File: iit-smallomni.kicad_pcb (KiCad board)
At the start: 2 copper layers, 100 x 100 mm, 87 parts, among them J1 Battery, J10 DC-Motor, J2 HC_SR04, J3 HC_SR04, J4 HC_SR04, J5 DC-Motor, J6 DC-Motor, J7 DC-Motor, J8 DC-Motor, J9 DC-Motor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

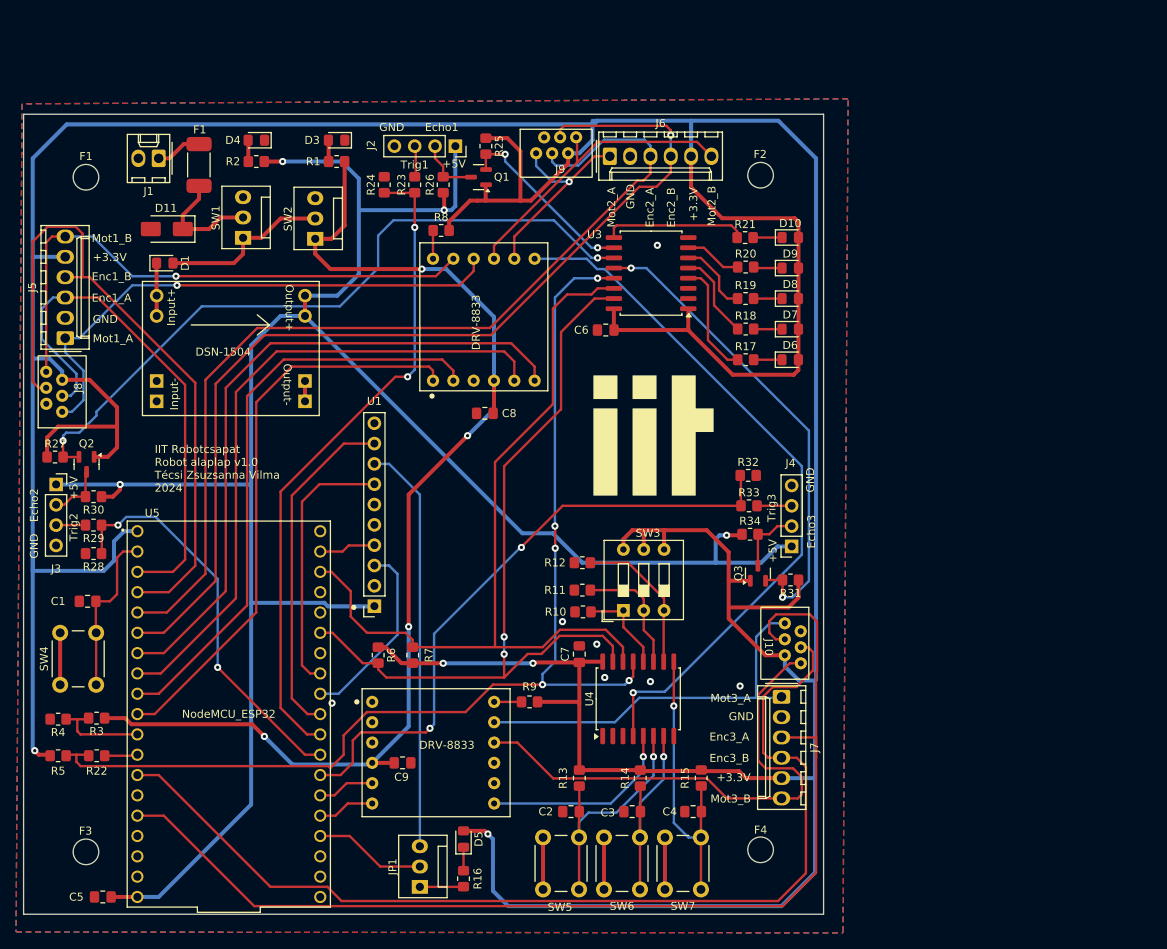
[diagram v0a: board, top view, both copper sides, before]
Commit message: Clean up names, schematic grid and files
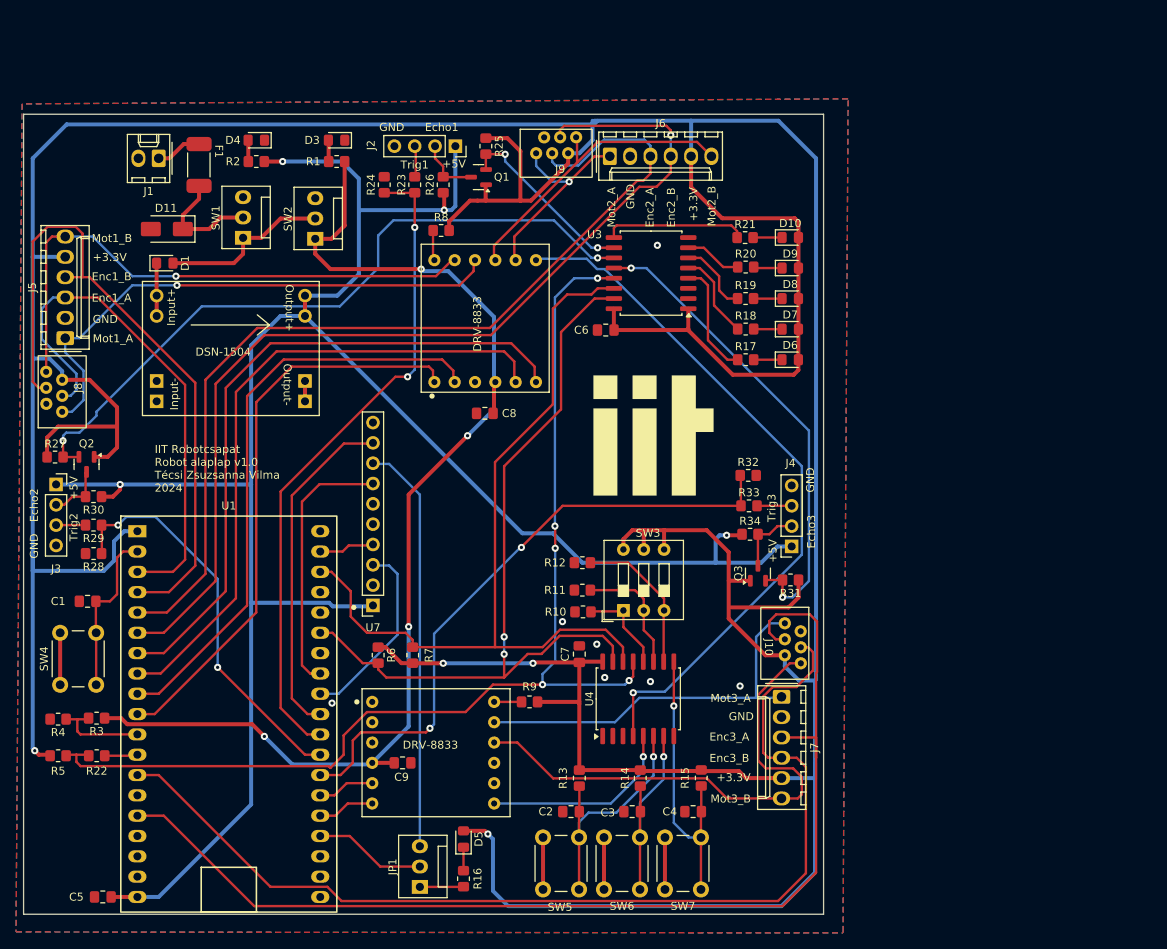
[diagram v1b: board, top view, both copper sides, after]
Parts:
- removed the F1 at (122.1, 34.9)
- removed F2, F3, F4: MountingHole_3.2mm_M3, MountingHole:MountingHole_3.2mm_M3
- F1: footprint Onlab:polyfuse -> iit-smallomni:polyfuse
- J10, J8, J9: footprint Onlab:motor -> iit-smallomni:motor
- R1: value 502.5 -> 10k
- R16, R17, R18, R19, R20, R21: value 68 -> 1k
- R2: value 152.5 -> 3k
- R3: value 7.5k -> 9.1k
- R4: value 2.5k -> 3k
- U1: value MPU-9250_IMU -> NodeMCU_ESP32; footprint Connector_PinSocket_2.54mm:PinSocket_1x10_P2.54mm_Vertical -> iit-smallomni:NodeMCU32S
- U2: footprint Onlab:DSN1504_module -> iit-smallomni:DSN1504_module
- U5: value NodeMCU_ESP32 -> DRV-8833_module; footprint NodeMCU_ESP32:MODULE_NODEMCU-32S -> iit-smallomni:DRV-8833_module
- U6: footprint Onlab:DRV-8833_module -> iit-smallomni:DRV-8833_module
- U7: value DRV-8833_module -> MPU-9250_IMU; footprint Onlab:DRV-8833_module -> Connector_PinSocket_2.54mm:PinSocket_1x10_P2.54mm_Vertical
- moved U5 57.4 mm to (171.6, 54.1), turned to 90 degrees
- moved U7 37.0 mm to (158.0, 88.4), turned to 180 degrees
- moved U1 22.7 mm to (140.0, 102.0), turned to 0 degrees
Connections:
- C1 pad 1: Net-(U5-EN/RESET) -> Net-(U1-EN/RESET)
- R22 pad 2: Net-(U5-P14/GPIO14/ADC2_CH6) -> Net-(U1-P14/GPIO14/ADC2_CH6)
- R8 pad 2: Net-(U7-EEP) -> Net-(U5-EEP)
- SW4 pad 2: Net-(U5-EN/RESET) -> Net-(U1-EN/RESET)
- U1 pad 1: +5V -> +3.3V
- U1 pad 10: GND -> /Mot1_DrvA
- U1 pad 2: GND -> Net-(U1-EN/RESET)
- U1 pad 3: /SCLK -> /Mot1_EncA
- U1 pad 4: /MOSI -> /Mot1_EncB
- U1 pad 5: unconnected-(U1-EDA-Pad5) -> /Mot2_EncA
- U1 pad 6: unconnected-(U1-ECL-Pad6) -> /Mot2_EncB
- U1 pad 7: /MISO -> /Mot2_DrvB
- U1 pad 8: /MPU95 interrupt -> /Mot2_DrvA
- U1 pad 9: /nCS -> /Mot1_DrvB
- U5 pad 1: +3.3V -> /Mot1_DrvA
- U5 pad 10: /Mot1_DrvA -> /Mot1_A
- U5 pad 11: /Battery level -> /Mot1_B
- U5 pad 12: Net-(U5-P14/GPIO14/ADC2_CH6) -> Net-(U5-EEP)
- U5 pad 2: Net-(U5-EN/RESET) -> /Mot1_DrvB
- U5 pad 3: /Mot1_EncA -> GND
- U5 pad 4: /Mot1_EncB -> VCC
- U5 pad 5: /Mot2_EncA -> /Mot2_DrvA
- U5 pad 6: /Mot2_EncB -> /Mot2_DrvB
- U5 pad 7: /Mot2_DrvB -> /DRV1_FAULT
- U5 pad 8: /Mot2_DrvA -> /Mot2_A
- U5 pad 9: /Mot1_DrvB -> /Mot2_B
- U7 pad 1: /Mot1_DrvA -> +5V
- U7 pad 10: /Mot1_A -> GND
- U7 pad 2: /Mot1_DrvB -> GND
- U7 pad 3: GND -> /SCLK
- U7 pad 4: VCC -> /MOSI
- U7 pad 5: /Mot2_DrvA -> unconnected-(U7-EDA-Pad5)
- U7 pad 6: /Mot2_DrvB -> unconnected-(U7-ECL-Pad6)
- U7 pad 7: /DRV1_FAULT -> /MISO
- U7 pad 8: /Mot2_A -> /MPU95 interrupt
- U7 pad 9: /Mot2_B -> /nCS
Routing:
- net Net-(U5-EN/RESET): track 20.9 -> 0.00 mm
- net Net-(U1-EN/RESET): track 0.00 -> 20.9 mm
- net Net-(U5-P14/GPIO14/ADC2_CH6): track 4.19 -> 0.00 mm
- net Net-(U1-P14/GPIO14/ADC2_CH6): track 0.00 -> 4.19 mm
- net Net-(U7-EEP): track 3.54 -> 0.00 mm
- net Net-(U5-EEP): track 0.00 -> 3.54 mm

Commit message: Fix flipped DRV8833
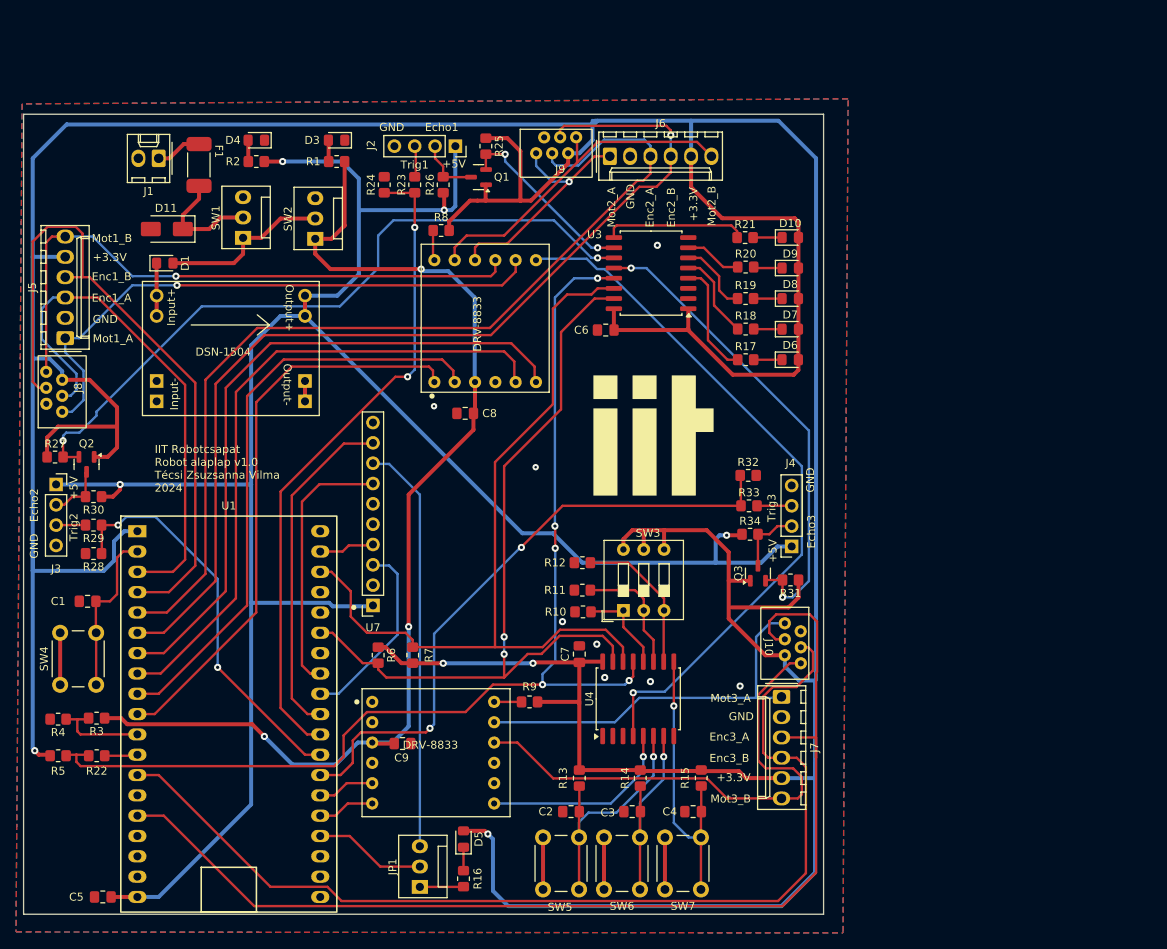
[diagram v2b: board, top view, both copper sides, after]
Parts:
- C1: value 10n -> 10u
- moved C8 2.46 mm to (169.5, 64.4)
- moved C9 2.41 mm to (161.7, 105.7)
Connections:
- U5 pad 10: /Mot1_A -> /Mot2_A
- U5 pad 11: /Mot1_B -> /Mot2_B
- U5 pad 3: GND -> VCC
- U5 pad 4: VCC -> GND
- U5 pad 8: /Mot2_A -> /Mot1_A
- U5 pad 9: /Mot2_B -> /Mot1_B
- U6 pad 3: GND -> VCC
- U6 pad 4: VCC -> GND
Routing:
- net /Mot1_B: track 70.3 -> 76.3 mm
- net VCC: track 144.7 -> 138.9 mm, vias 4 -> 3
- net /Mot1_A: track 68.0 -> 73.1 mm
- net /Mot2_B: track 38.2 -> 43.1 mm
- net /Mot2_A: track 25.4 -> 29.7 mm
- net GND: track 29.2 -> 28.8 mm, vias 7 -> 8

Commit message: Fix flipped DSN-1504
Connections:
- U2 pad 1: GND -> Net-(D1-K)
- U2 pad 2: Net-(D1-K) -> GND
- U2 pad 3: +5V -> GND
- U2 pad 4: GND -> +5V
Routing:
- net Net-(D1-K): track 6.61 -> 19.7 mm, vias 0 -> 1
- net +5V: track 269.3 -> 263.2 mm
- net /UV_Trig_2: track 89.7 -> 94.1 mm
- net GND: track 28.8 -> 26.2 mm, vias 8 -> 10

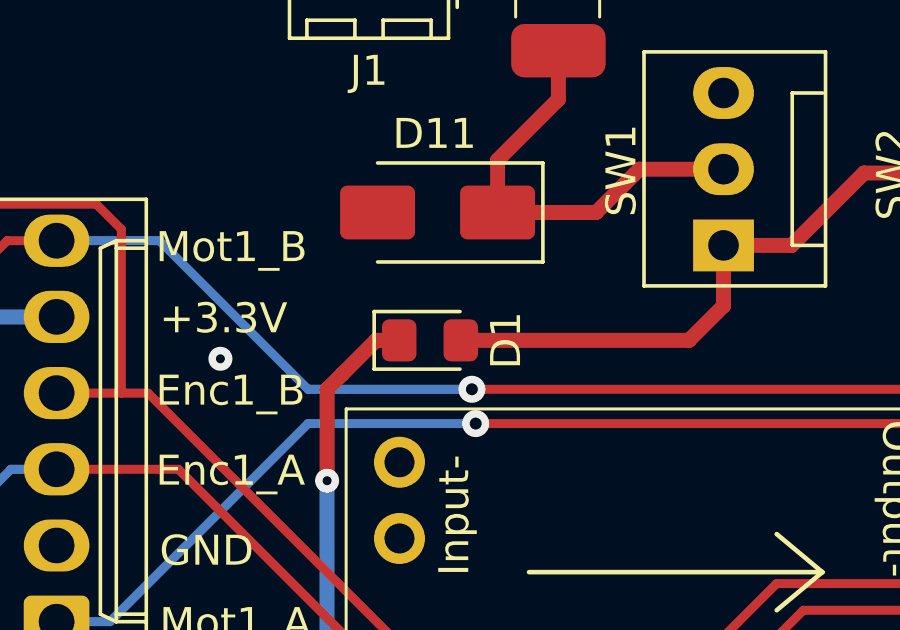
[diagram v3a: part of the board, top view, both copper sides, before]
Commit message: Update Schottky diode footprint in design
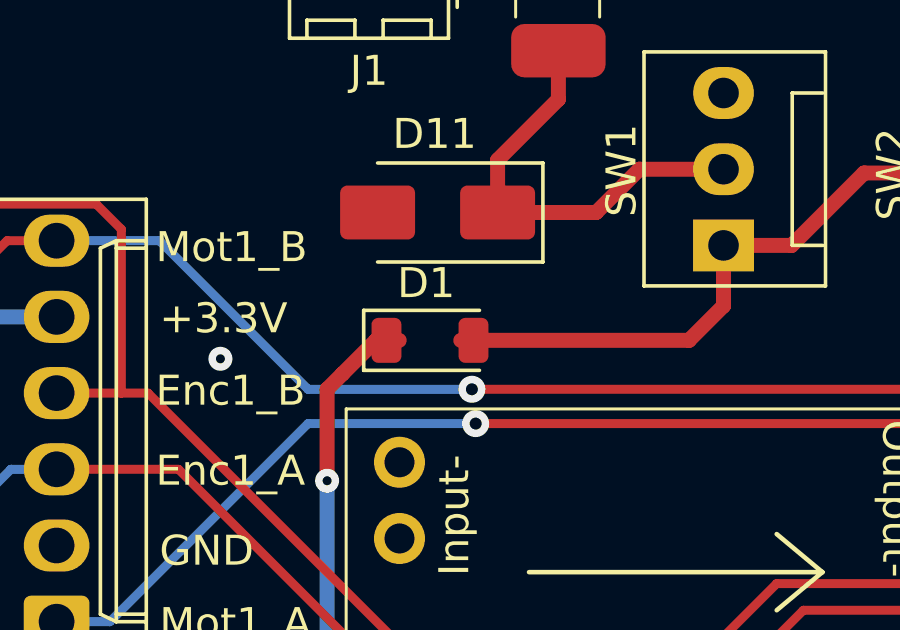
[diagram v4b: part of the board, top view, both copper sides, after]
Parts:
- D1: footprint Diode_SMD:D_0805_2012Metric_Pad1.15x1.40mm_HandSolder -> iit-smallomni:D_SOD-123FL
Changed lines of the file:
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@@
 		)
 	)
-	(footprint "Diode_SMD:D_0805_2012Metric_Pad1.15x1.40mm_HandSolder"
+	(footprint "iit-smallomni:D_SOD-123FL"
 		(layer "F.Cu")
 		(at 131.953 45.613)
-		(descr "Diode SMD 0805 (2012 Metric), square (rectangular) end terminal, IPC_7351 nominal, (Body size source: https://docs.google.com/spreadsheets/d/1BsfQQcO9C6DZCsRaXUlFlo91Tg2WpOkGARC1WS5S8t0/edit?usp=sharing), generated with kicad-footprint-generator")
-		(tags "diode handsolder")
+		(descr "D_SOD-123F")
+		(tags "D_SOD-123F")
 		(property "Reference" "D1"
-			(at 2.54 0 90)
-			(layer "F.SilkS")
-			(effects
-				(font
-					(size 1 1)
-					(thickness 0.153)
-				)
-			)
-		)
-		(property "Value" "D_Schottky"
-			(at 0 1.65 0)
-			(layer "F.Fab")
+			(at -0.127 -1.905 0)
+			(layer "F.SilkS")
 			(effects
 				(font
@@
 			)
 		)
-		(property "Footprint" "Diode_SMD:D_0805_2012Metric_Pad1.15x1.40mm_HandSolder"
+		(property "Value" "D_Schottky"
+			(at 0 2.1 0)
+			(layer "F.Fab")
+			(effects
+				(font
+					(size 1 1)
+					(thickness 0.15)
+				)
+			)
+		)
+		(property "Footprint" "iit-smallomni:D_SOD-123FL"
 			(at 0 0 0)
+			(unlocked yes)
 			(layer "F.Fab")
 			(hide yes)
@@
 				(font
 					(size 1.27 1.27)
-					(thickness 0.15)
 				)
 			)
@@
 		(property "Datasheet" ""
 			(at 0 0 0)
+			(unlocked yes)
 			(layer "F.Fab")
 			(hide yes)
@@
 				(font
 					(size 1.27 1.27)
-					(thickness 0.15)
 				)
 			)
@@
 		(property "Description" "Schottky diode"
 			(at 0 0 0)
+			(unlocked yes)
 			(layer "F.Fab")
 			(hide yes)
@@
 				(font
 					(size 1.27 1.27)
-					(thickness 0.15)
 				)
 			)
@@
 		(attr smd)
 		(fp_line
-			(start -1.86 -0.96)
-			(end -1.86 0.96)
+			(start -2.21 -1)
+			(end -2.21 1)
 			(stroke
 				(width 0.12)
@@
 		)
 		(fp_line
-			(start -1.86 0.96)
-			(end 1 0.96)
+			(start -2.21 -1)
+			(end 1.65 -1)
 			(stroke
 				(width 0.12)
@@
 		)
 		(fp_line
-			(start 1 -0.96)
-			(end -1.86 -0.96)
+			(start -2.21 1)
+			(end 1.65 1)
 			(stroke
 				(width 0.12)
@@
 		)
 		(fp_line
-			(start -1.85 -0.95)
-			(end 1.85 -0.95)
-			(stroke
-				(width 0.05)
-				(type solid)
-			)
-			(layer "F.CrtYd")
-		)
-		(fp_line
-			(start -1.85 0.95)
-			(end -1.85 -0.95)
-			(stroke
-				(width 0.05)
-				(type solid)
-			)
-			(layer "F.CrtYd")
-		)
-		(fp_line
-			(start 1.85 -0.95)
-			(end 1.85 0.95)
-			(stroke
-				(width 0.05)
-				(type solid)
-			)
-			(layer "F.CrtYd")
-		)
-		(fp_line
-			(start 1.85 0.95)
-			(end -1.85 0.95)
-			(stroke
-				(width 0.05)
-				(type solid)
-			)
-			(layer "F.CrtYd")
-		)
-		(fp_line
-			(start -1 -0.3)
-			(end -1 0.6)
-			(stroke
-				(width 0.1)
-				(type solid)
-			)
-			(layer "F.Fab")
-		)
-		(fp_line
-			(start -1 0.6)
-			(end 1 0.6)
-			(stroke
-				(width 0.1)
-				(type solid)
-			)
-			(layer "F.Fab")
-		)
-		(fp_line
-			(start -0.7 -0.6)
-			(end -1 -0.3)
-			(stroke
-				(width 0.1)
-				(type solid)
-			)
-			(layer "F.Fab")
-		)
-		(fp_line
-			(start 1 -0.6)
-			(end -0.7 -0.6)
-			(stroke
-				(width 0.1)
-				(type solid)
-			)
-			(layer "F.Fab")
-		)
-		(fp_line
-			(start 1 0.6)
-			(end 1 -0.6)
+			(start -2.2 -1.15)
+			(end -2.2 1.15)
+			(stroke
+				(width 0.05)
+				(type solid)
+			)
+			(layer "F.CrtYd")
+		)
+		(fp_line
+			(start -2.2 -1.15)
+			(end 2.2 -1.15)
+			(stroke
+				(width 0.05)
+				(type solid)
+			)
+			(layer "F.CrtYd")
+		)
+		(fp_line
+			(start 2.2 -1.15)
+			(end 2.2 1.15)
+			(stroke
+				(width 0.05)
+				(type solid)
+			)
+			(layer "F.CrtYd")
+		)
+		(fp_line
+			(start 2.2 1.15)
+			(end -2.2 1.15)
+			(stroke
+				(width 0.05)
+				(type solid)
+			)
+			(layer "F.CrtYd")
+		)
+		(fp_line
+			(start -1.45 -0.9)
+			(end 1.45 -0.9)
+			(stroke
+				(width 0.1)
+				(type solid)
+			)
+			(layer "F.Fab")
+		)
+		(fp_line
+			(start -1.45 0.9)
+			(end -1.45 -0.9)
+			(stroke
+				(width 0.1)
+				(type solid)
+			)
+			(layer "F.Fab")
+		)
+		(fp_line
+			(start -0.75 0)
+			(end -0.35 0)
+			(stroke
+				(width 0.1)
+				(type solid)
+			)
+			(layer "F.Fab")
+		)
+		(fp_line
+			(start -0.35 0)
+			(end -0.35 -0.55)
+			(stroke
+				(width 0.1)
+				(type solid)
+			)
+			(layer "F.Fab")
+		)
+		(fp_line
+			(start -0.35 0)
+			(end -0.35 0.55)
+			(stroke
+				(width 0.1)
+				(type solid)
+			)
+			(layer "F.Fab")
+		)
+		(fp_line
+			(start -0.35 0)
+			(end 0.25 -0.4)
+			(stroke
+				(width 0.1)
+				(type solid)
+			)
+			(layer "F.Fab")
+		)
+		(fp_line
+			(start 0.25 -0.4)
+			(end 0.25 0.4)
+			(stroke
+				(width 0.1)
+				(type solid)
+			)
+			(layer "F.Fab")
+		)
+		(fp_line
+			(start 0.25 0)
+			(end 0.75 0)
+			(stroke
+				(width 0.1)
+				(type solid)
+			)
+			(layer "F.Fab")
+		)
+		(fp_line
+			(start 0.25 0.4)
+			(end -0.35 0)
+			(stroke
+				(width 0.1)
+				(type solid)
+			)
+			(layer "F.Fab")
+		)
+		(fp_line
+			(start 1.45 -0.9)
+			(end 1.45 0.9)
+			(stroke
+				(width 0.1)
+				(type solid)
+			)
+			(layer "F.Fab")
+		)
+		(fp_line
+			(start 1.45 0.9)
+			(end -1.45 0.9)
 			(stroke
 				(width 0.1)
@@
 		)
 		(fp_text user "${REFERENCE}"
-			(at 0 0 0)
-			(layer "F.Fab")
-			(effects
-				(font
-					(size 0.5 0.5)
-					(thickness 0.08)
+			(at -0.127 -1.905 0)
+			(layer "F.Fab")
+			(effects
+				(font
+					(size 1 1)
+					(thickness 0.15)
 				)
 			)
 		)
 		(pad "1" smd roundrect
-			(at -1.025 0)
-			(size 1.15 1.4)
+			(at -1.45 0)
+			(size 1 1.5)
 			(layers "F.Cu" "F.Paste" "F.Mask")
-			(roundrect_rratio 0.2173913043)
+			(roundrect_rratio 0.2272727273)
 			(net 8 "Net-(D1-K)")
 			(pinfunction "K")
@@
 		)
 		(pad "2" smd roundrect
-			(at 1.025 0)
-			(size 1.15 1.4)
+			(at 1.45 0)
+			(size 1 1.5)
 			(layers "F.Cu" "F.Paste" "F.Mask")
-			(roundrect_rratio 0.2173913043)
+			(roundrect_rratio 0.2272727273)
 			(net 9 "Net-(D1-A)")
 			(pinfunction "A")
 			(pintype "passive")
 		)
-		(model "${KICAD6_3DMODEL_DIR}/Diode_SMD.3dshapes/D_0805_2012Metric.wrl"
+		(model "${KICAD8_3DMODEL_DIR}/Diode_SMD.3dshapes/D_SOD-123F.wrl"
 			(offset
 				(xyz 0 0 0)

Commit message: Fix motor connector layout
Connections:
- J10 pad 2: GND -> /Mot3_B
- J10 pad 3: /Mot3_EncA -> GND
- J10 pad 4: /Mot3_EncB -> +3.3V
- J10 pad 5: +3.3V -> /Mot3_EncA
- J10 pad 6: /Mot3_B -> /Mot3_EncB
- J8 pad 2: GND -> /Mot1_B
- J8 pad 3: /Mot1_EncA -> GND
- J8 pad 4: /Mot1_EncB -> +3.3V
- J8 pad 5: +3.3V -> /Mot1_EncA
- J8 pad 6: /Mot1_B -> /Mot1_EncB
- J9 pad 2: GND -> /Mot2_B
- J9 pad 3: /Mot2_EncA -> GND
- J9 pad 4: /Mot2_EncB -> +3.3V
- J9 pad 5: +3.3V -> /Mot2_EncA
- J9 pad 6: /Mot2_B -> /Mot2_EncB
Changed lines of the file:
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@@
 			(layers "*.Cu" "*.Mask")
 			(remove_unused_layers no)
-			(net 1 "GND")
+			(net 28 "/Mot1_B")
 			(pinfunction "Pin_2")
 			(pintype "passive")
@@
 			(layers "*.Cu" "*.Mask")
 			(remove_unused_layers no)
-			(net 26 "/Mot1_EncA")
+			(net 1 "GND")
 			(pinfunction "Pin_3")
 			(pintype "passive")
@@
 			(layers "*.Cu" "*.Mask")
 			(remove_unused_layers no)
-			(net 27 "/Mot1_EncB")
+			(net 6 "+3.3V")
 			(pinfunction "Pin_4")
 			(pintype "passive")
@@
 			(layers "*.Cu" "*.Mask")
 			(remove_unused_layers no)
-			(net 6 "+3.3V")
+			(net 26 "/Mot1_EncA")
 			(pinfunction "Pin_5")
 			(pintype "passive")
@@
 			(layers "*.Cu" "*.Mask")
 			(remove_unused_layers no)
-			(net 28 "/Mot1_B")
+			(net 27 "/Mot1_EncB")
 			(pinfunction "Pin_6")
 			(pintype "passive")
@@
 			(layers "*.Cu" "*.Mask")
 			(remove_unused_layers no)
-			(net 1 "GND")
+			(net 32 "/Mot2_B")
 			(pinfunction "Pin_2")
 			(pintype "passive")
@@
 			(layers "*.Cu" "*.Mask")
 			(remove_unused_layers no)
-			(net 30 "/Mot2_EncA")
+			(net 1 "GND")
 			(pinfunction "Pin_3")
 			(pintype "passive")
@@
 			(layers "*.Cu" "*.Mask")
 			(remove_unused_layers no)
-			(net 31 "/Mot2_EncB")
+			(net 6 "+3.3V")
 			(pinfunction "Pin_4")
 			(pintype "passive")
@@
 			(layers "*.Cu" "*.Mask")
 			(remove_unused_layers no)
-			(net 6 "+3.3V")
+			(net 30 "/Mot2_EncA")
 			(pinfunction "Pin_5")
 			(pintype "passive")
@@
 			(layers "*.Cu" "*.Mask")
 			(remove_unused_layers no)
-			(net 32 "/Mot2_B")
+			(net 31 "/Mot2_EncB")
 			(pinfunction "Pin_6")
 			(pintype "passive")
@@
 			(layers "*.Cu" "*.Mask")
 			(remove_unused_layers no)
-			(net 1 "GND")
+			(net 36 "/Mot3_B")
 			(pinfunction "Pin_2")
 			(pintype "passive")
@@
 			(layers "*.Cu" "*.Mask")
 			(remove_unused_layers no)
-			(net 34 "/Mot3_EncA")
+			(net 1 "GND")
 			(pinfunction "Pin_3")
 			(pintype "passive")
@@
 			(layers "*.Cu" "*.Mask")
 			(remove_unused_layers no)
-			(net 35 "/Mot3_EncB")
+			(net 6 "+3.3V")
 			(pinfunction "Pin_4")
 			(pintype "passive")
@@
 			(layers "*.Cu" "*.Mask")
 			(remove_unused_layers no)
-			(net 6 "+3.3V")
+			(net 34 "/Mot3_EncA")
 			(pinfunction "Pin_5")
 			(pintype "passive")
@@
 			(layers "*.Cu" "*.Mask")
 			(remove_unused_layers no)
-			(net 36 "/Mot3_B")
+			(net 35 "/Mot3_EncB")
 			(pinfunction "Pin_6")
 			(pintype "passive")
@@
 		(min_thickness 0.25)
 		(filled_areas_thickness no)
-		(fill yes
+		(fill
 			(thermal_gap 0.5)
 			(thermal_bridge_width 0.5)
